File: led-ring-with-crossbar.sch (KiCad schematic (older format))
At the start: 88 parts

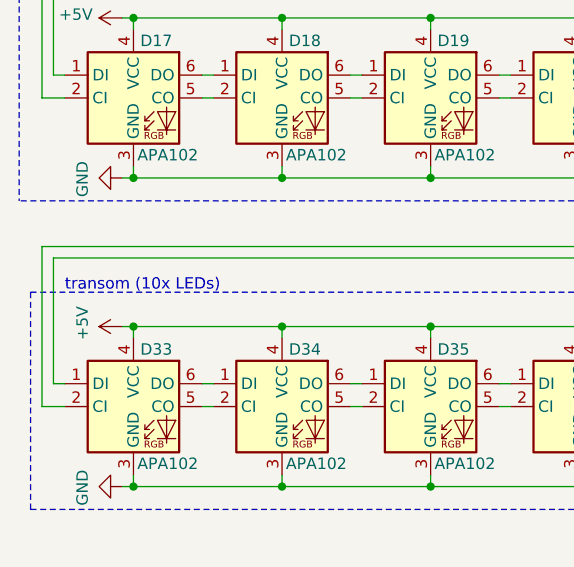
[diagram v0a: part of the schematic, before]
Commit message: Rename transom to crossbar
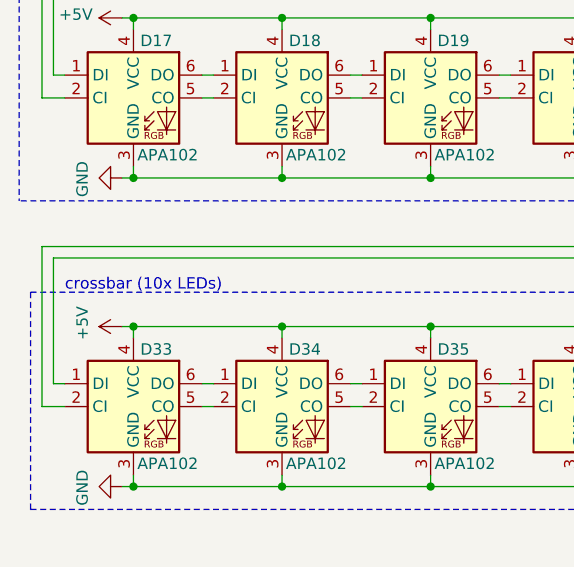
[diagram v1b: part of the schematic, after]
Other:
- note added: "crossbar (10x LEDs)"
- note removed: "transom (10x LEDs)"
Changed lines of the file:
@@
 decoupling
 Text Notes 700  3150 0    50   ~ 0
-transom (10x LEDs)
+crossbar (10x LEDs)
 $Comp
 L Connector:Conn_01x04_Male J_OUT1
